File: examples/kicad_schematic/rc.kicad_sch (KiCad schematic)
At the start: 3 parts

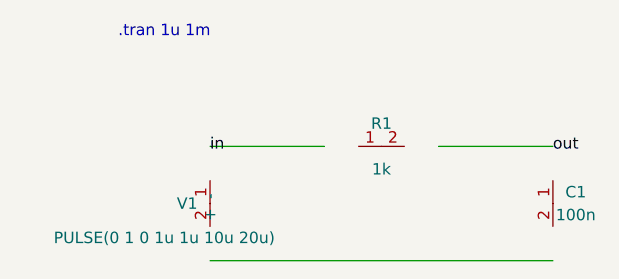
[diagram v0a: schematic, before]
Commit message: Import KiCad schematics through Rust IR
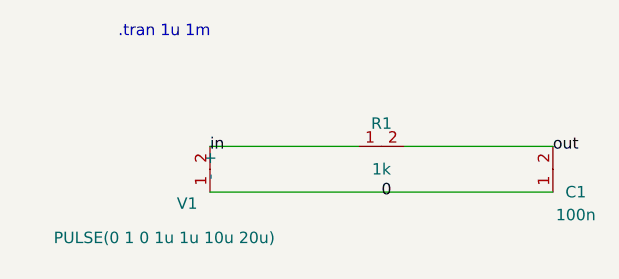
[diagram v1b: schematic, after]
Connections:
- net in: now also R1.1, V1.2 (-)
- net out: now also C1.2, R1.2
- net 0: now reaches V1.1 (+)
- net 0: now also C1.1
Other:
- moved on the sheet: C1, V1
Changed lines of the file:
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@@
   (generator "NekoSpice")
   (paper "A4")
-  (wire (pts (xy 50.8 50.8) (xy 63.5 50.8)) (stroke (width 0) (type default)))
-  (wire (pts (xy 76.2 50.8) (xy 88.9 50.8)) (stroke (width 0) (type default)))
-  (wire (pts (xy 88.9 63.5) (xy 50.8 63.5)) (stroke (width 0) (type default)))
+  (wire (pts (xy 50.8 50.8) (xy 67.31 50.8)) (stroke (width 0) (type default)))
+  (wire (pts (xy 72.39 50.8) (xy 88.9 50.8)) (stroke (width 0) (type default)))
+  (wire (pts (xy 88.9 55.88) (xy 50.8 55.88)) (stroke (width 0) (type default)))
   (label "in" (at 50.8 50.8 0) (effects (font (size 1.27 1.27))))
   (label "out" (at 88.9 50.8 0) (effects (font (size 1.27 1.27))))
+  (label "0" (at 69.85 55.88 0) (effects (font (size 1.27 1.27))))
   (text ".tran 1u 1m" (at 45.72 38.1 0) (effects (font (size 1.27 1.27))))
   (symbol
     (lib_id "NekoSpice:V")
-    (at 50.8 57.15 0)
+    (at 50.8 53.34 0)
     (unit 1)
     (property "Reference" "V1" (at 48.26 57.15 0))
@@
   (symbol
     (lib_id "NekoSpice:C")
-    (at 88.9 57.15 0)
+    (at 88.9 53.34 0)
     (unit 1)
     (property "Reference" "C1" (at 91.44 55.88 0))
